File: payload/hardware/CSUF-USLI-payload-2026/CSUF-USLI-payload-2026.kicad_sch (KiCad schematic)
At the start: 5 parts, among them U1 DEV-16771, U2 GPS6MV2

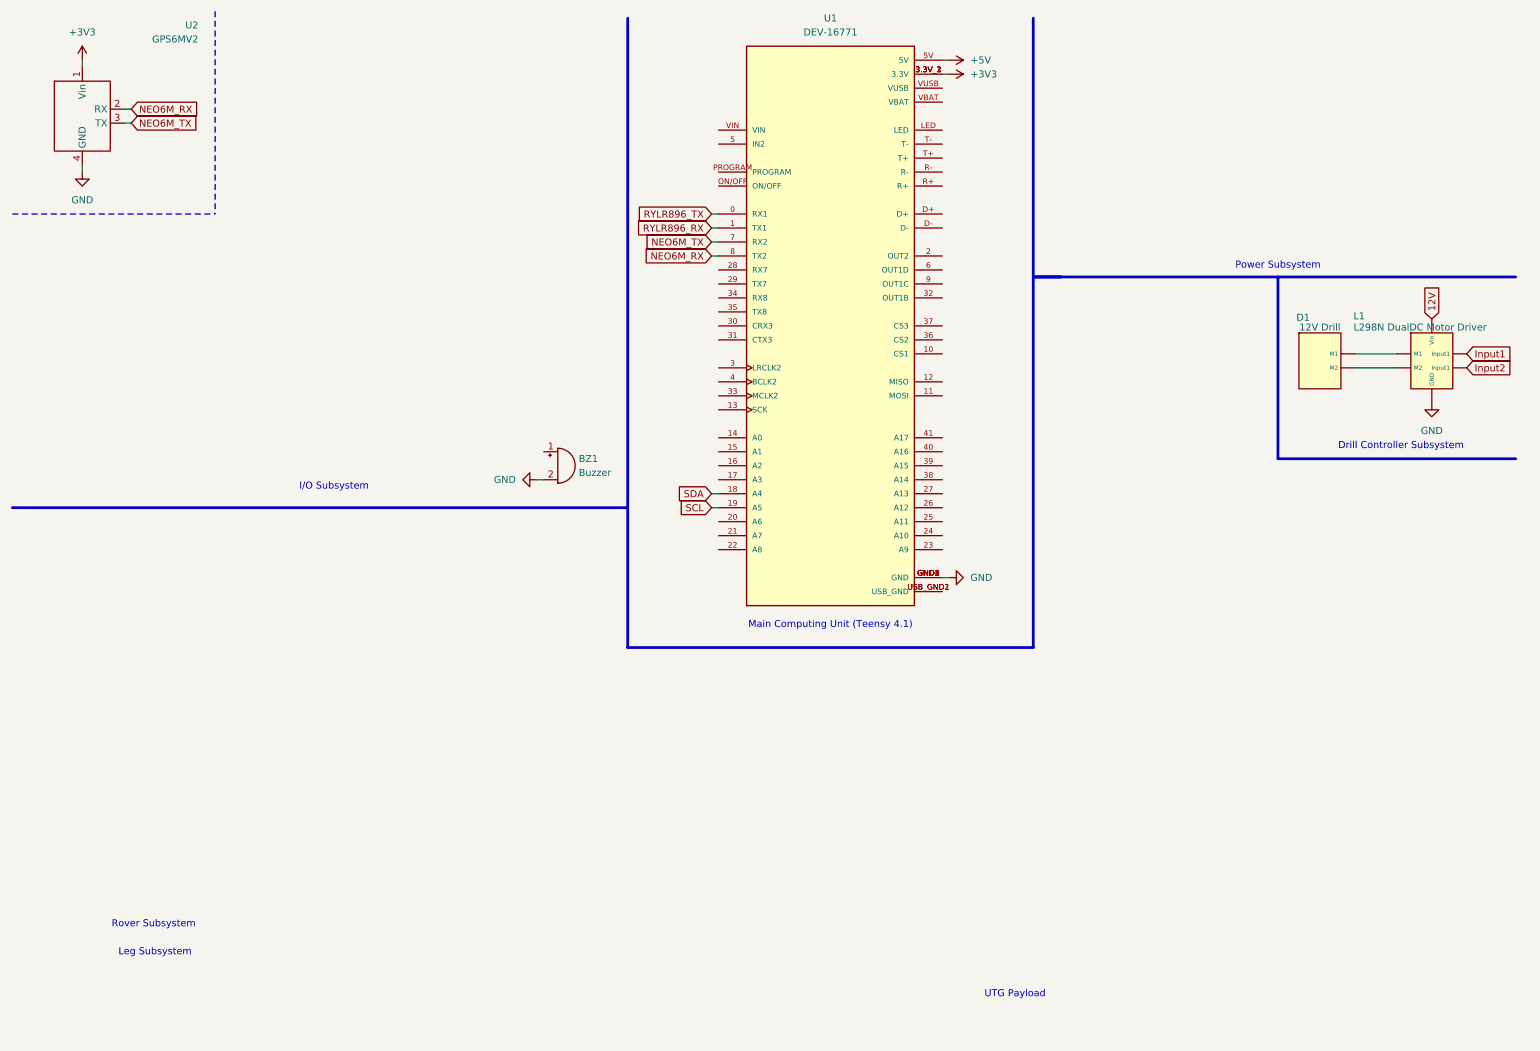
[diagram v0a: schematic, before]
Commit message: Rover Subsystem
Created "generic" symbol library to hold generic symbols (including the 12v drill created earlier)
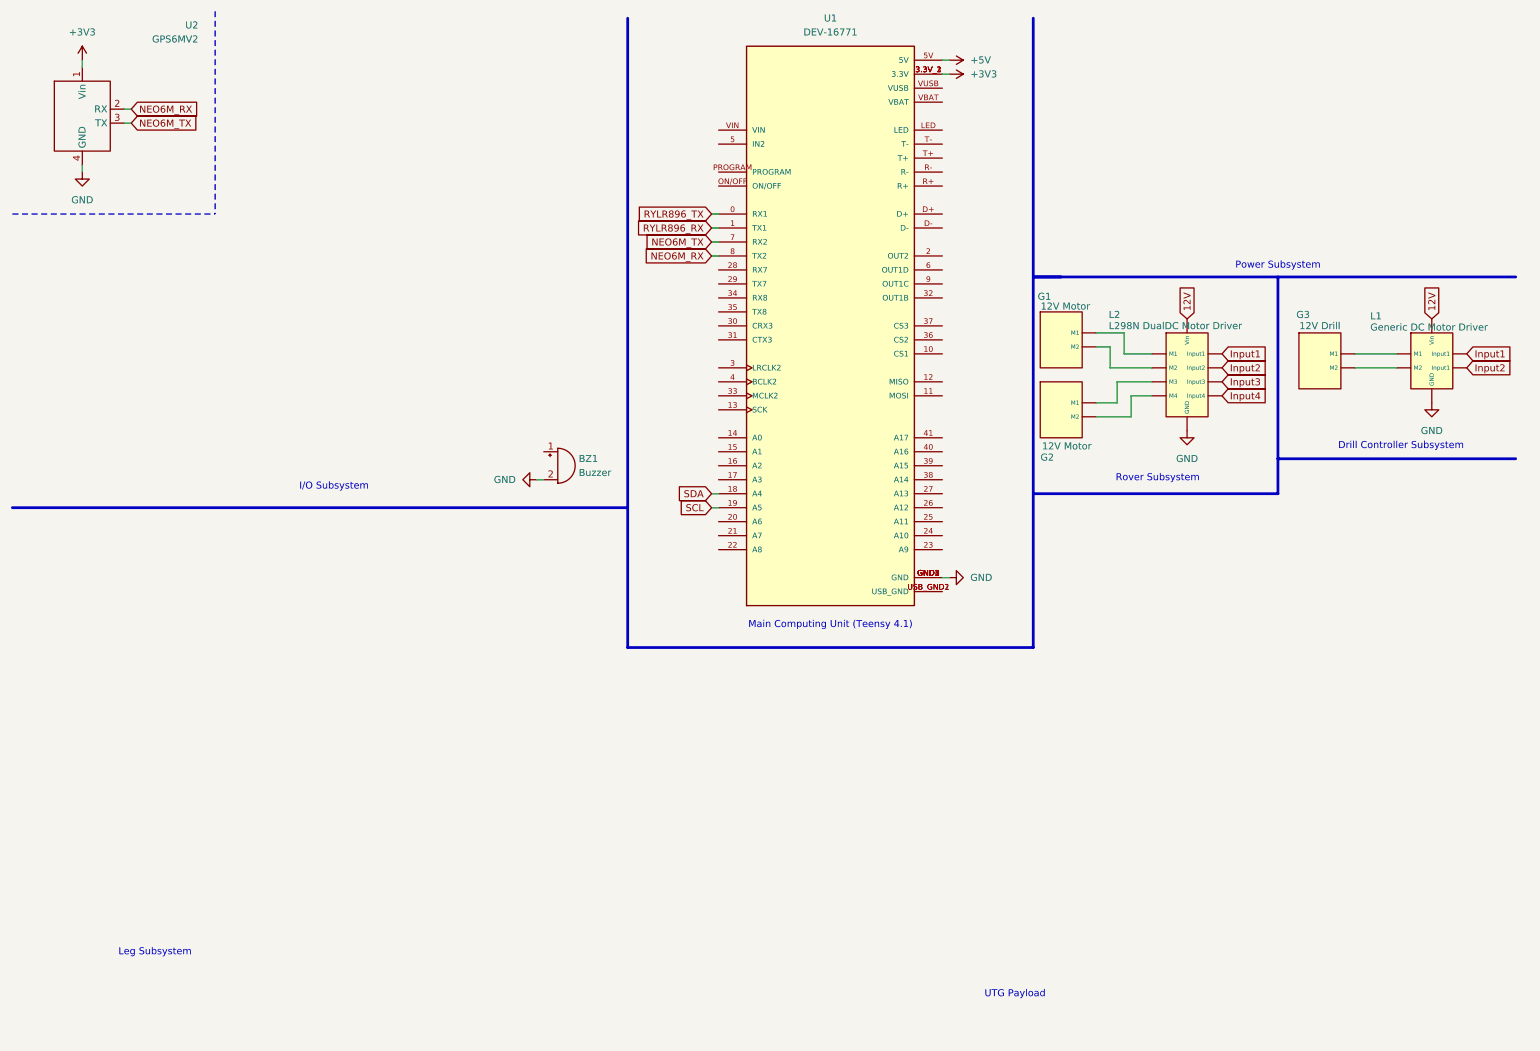
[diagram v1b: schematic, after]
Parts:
- removed D1: 12V Drill, symbol L298N Concept:12V_Drill
- added G1, G2: 12V Motor, symbol Generic Devices:12V_Motor
- added G3: 12V Drill, symbol Generic Devices:12V_Drill
- added L2: L298N DualDC Motor Driver, symbol L298N Concept:L298N
- L1: value L298N DualDC Motor Driver -> Generic DC Motor Driver
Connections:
- net 12V: now also L2. (Input4)
- net GND: now also L2. (Input4)
- net Input1: now also L2. (Input4)
- net Input2: now also L2. (Input4)
- new net: G1. (M2), L2. (Input4) (x2)
- new net: G2. (M2), L2. (Input4) (x2)
- new net: G3. (M2), L1. (Input1) (x2)
- new net Input3: L2. (Input4)
- new net Input4: L2. (Input4)

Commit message: KiCad does not like merge requests
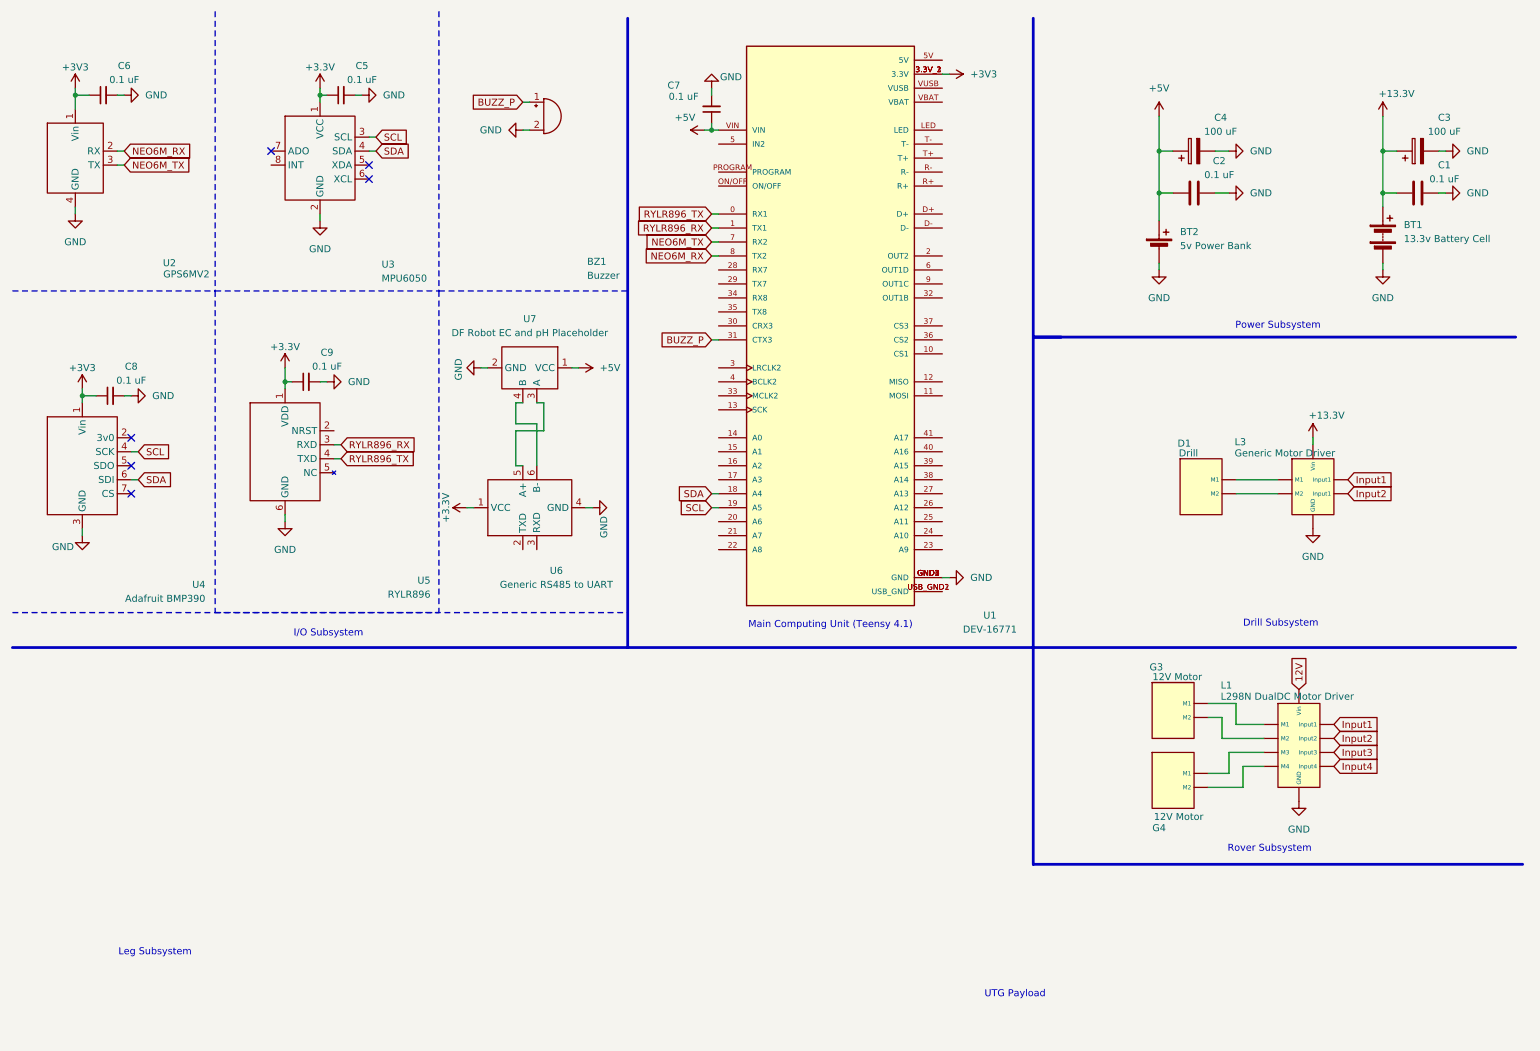
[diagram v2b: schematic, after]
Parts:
- removed G1, G2: 12V Motor, symbol Generic Devices:12V_Motor
- removed G3: 12V Drill, symbol Generic Devices:12V_Drill
- removed L2: L298N DualDC Motor Driver, symbol L298N Concept:L298N
- added BT1: 13.3v Battery Cell, symbol Device:Battery
- added BT2: 5v Power Bank, symbol Device:Battery_Cell
- added C1, C2: 0.1 uF, symbol Device:C
- added C3, C4: 100 uF, symbol Device:C_Polarized
- added C5, C6, C7, C8, C9: 0.1 uF, symbol Device:C_Small
- added D1: Drill, symbol L298N Concept:12V_Drill
- added G3, G4: 12V Motor, symbol Generic Devices:12V_Motor
- added L3: Generic Motor Driver, symbol L298N Concept:L298N
- added U3: MPU6050, symbol MPU6050:MPU6050
- added U4: Adafruit BMP390, symbol BMP280:Adafruit_BMP280
- added U5: RYLR896, symbol RYLR896:RYLR896
- added U6: Generic RS485 to UART, symbol RS485_to_UART:Generic_RS485_to_UART
- added U7: DF Robot EC and pH Placeholder, symbol Soil_Sensors:DFRobot_EC_and_pH
- L1: value Generic DC Motor Driver -> L298N DualDC Motor Driver
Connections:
- net +3V3: now also C6.1, C8.1, U4.1 (Vin)
- net +5V: now also U1.VIN, BT2.1 (+), C2.1, C4.1, C7.1, U7.1 (VCC); no longer U1.5V
- net GND: now also BT1.2 (-), BT2.2 (-), C1.2, C2.2, C3.2, C4.2, C5.2, C6.2, C7.2, C8.2, C9.2, L3. (Input1), U3.2 (GND), U4.3 (GND), U5.6 (GND), U6.4 (GND), U7.2 (GND)
- net Input1: now also L3. (Input1)
- net Input2: now also L3. (Input1)
- net Input3: now also L1. (Input4)
- net Input4: now also L1. (Input4)
- net RYLR896_RX: now also U5.3 (RXD)
- net RYLR896_TX: now also U5.4 (TXD)
- net SCL: now also U3.3 (SCL), U4.4 (SCK)
- net SDA: now also U3.4 (SDA), U4.6 (SDI)
- net BUZZ_P: now reaches U1.31 (CTX3)
- net BUZZ_P: now also BZ1.1 (+)
- new net: D1. (M2), L3. (Input1) (x2)
- new net: U6.5 (A+), U7.3 (A)
- new net: U6.6 (B-), U7.4 (B)
- new net: G3. (M2), L1. (Input4) (x2)
- new net: G4. (M2), L1. (Input4) (x2)
- new net +13.3V: BT1.1 (+), C1.1, C3.1, L3. (Input1)
- new net +3.3V: C5.1, C9.1, U3.1 (VCC), U5.1 (VDD), U6.1 (VCC)
- no-connect marks 0 -> 6
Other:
- note added: "Drill Subsystem"
- note removed: "Drill Controller Subsystem"
- moved on the sheet: BZ1, U2

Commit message: Update CSUF-USLI-payload-2026.kicad_sch
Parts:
- added M1: Motor_Servo, symbol Motor:Motor_Servo
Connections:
- net 12V is gone; now on net ROVER_IN4: L1. (Input4)
- net Input3 is gone; now on net ROVER_IN4: L1. (Input4)
- net Input4 is gone; now on net ROVER_IN4: L1. (Input4)
- net +13.3V: now also L1. (Input4), M1.2 (+)
- net GND: now also M1.3 (-)
- net LEG_PWM: now reaches U1.14 (A0)
- net LEG_PWM: now also M1.1 (PWM)
- net SOIL_TX: now reaches U1.28 (RX7)
- net SOIL_TX: now also U6.2 (TXD)
- net SOIL_RX: now reaches U1.29 (TX7)
- net SOIL_RX: now also U6.3 (RXD)
- net ROVER_IN4: now reaches L1. (Input4)
- net ROVER_IN4: no longer G3. (M2)
- removed net Input1: L1. (Input4), L3. (Input1)
- removed net Input2: L1. (Input4), L3. (Input1)
- new net: D1. (M2), L3. (Input1)
- new net: G3. (M2), L1. (Input4)
- new net: G4. (M2), L1. (Input4)
- new net DRILL_IN1: L3. (Input1)
- new net DRILL_IN2: L3. (Input1)
- new net ROVER_IN1: L1. (Input4)
- new net ROVER_IN2: L1. (Input4)
- new net ROVER_IN3: L1. (Input4)
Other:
- note added: "Legs Subsystem"
- note removed: "Leg Subsystem"
- moved on the sheet: G3, G4, L1
